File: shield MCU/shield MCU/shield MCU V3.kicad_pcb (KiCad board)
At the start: 2 copper layers, 56 x 75.2 mm, 17 parts, among them J1 IR_sensor, J2 IR_sensor, J3 IR_sensor, J4 IR_sensor, J5 IR_sensor, J6 BATT, SW1 Pwr_Sw, U1 pwr_mgr_1, U3 gy50, U4 NUCLEO144-F429ZI

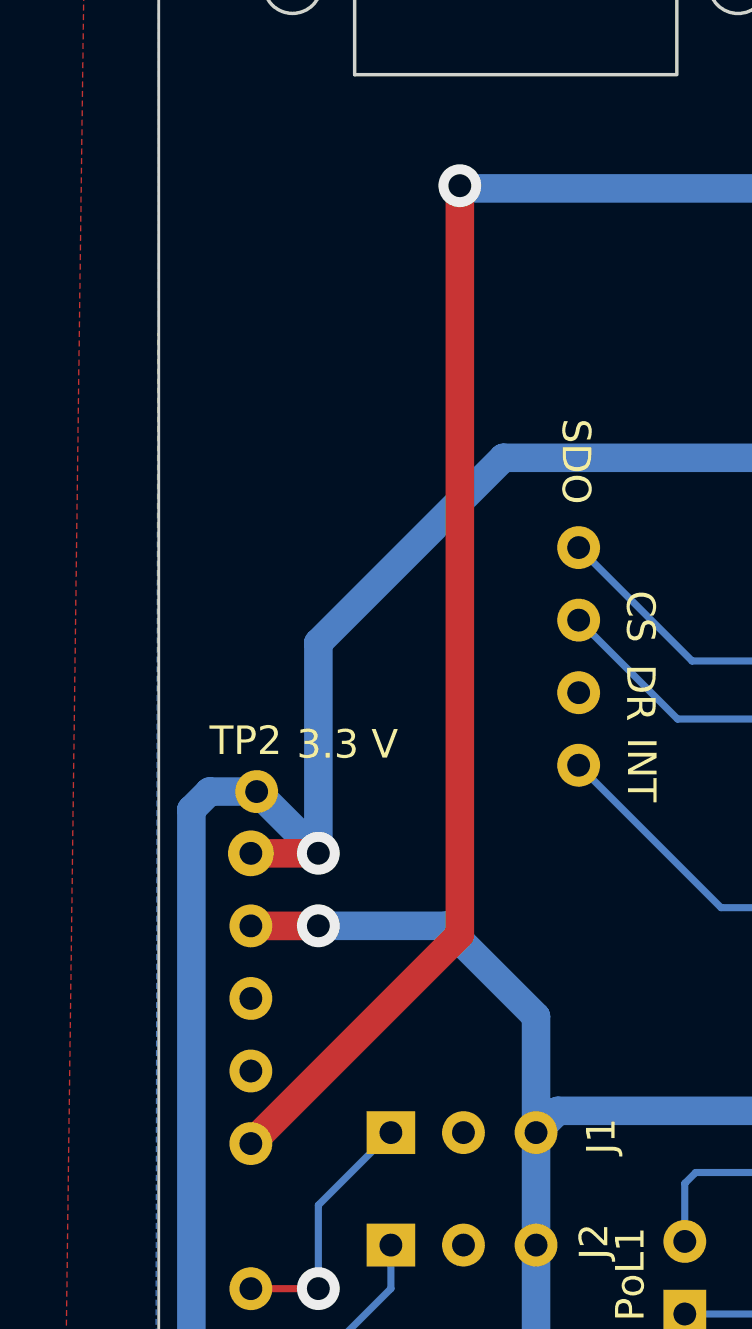
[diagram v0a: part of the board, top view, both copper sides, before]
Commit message: pcb V3 korjattu
ground korjattu
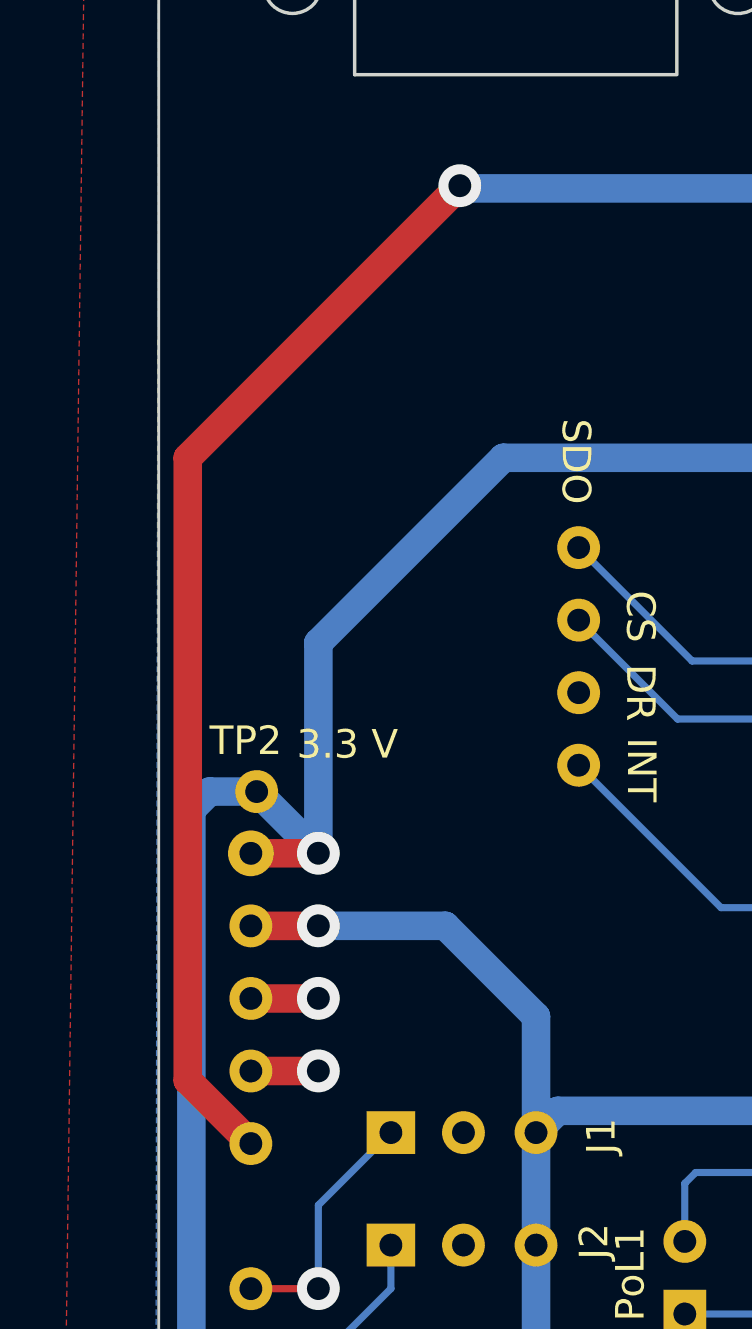
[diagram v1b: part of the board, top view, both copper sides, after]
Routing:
- net GND: track 0.00 -> 4.73 mm, vias 0 -> 2
- net /Vin: track 59.7 -> 61.6 mm
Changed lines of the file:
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@@
     (effects (font (size 1 1) (thickness 0.15)))
   )
+  (segment (start 108.582 110.366) (end 108.585 110.363) (width 1) (layer "F.Cu") (net 1))
+  (segment (start 106.2228 110.366) (end 108.582 110.366) (width 1) (layer "F.Cu") (net 1))
+  (segment (start 106.2228 107.826) (end 108.582 107.826) (width 1) (layer "F.Cu") (net 1))
+  (segment (start 108.582 107.826) (end 108.585 107.823) (width 1) (layer "F.Cu") (net 1))
+  (via (at 108.585 107.823) (size 1.5) (drill 0.8) (layers "F.Cu" "B.Cu") (free) (net 1))
+  (via (at 108.585 110.363) (size 1.5) (drill 0.8) (layers "F.Cu" "B.Cu") (free) (net 1))
   (segment (start 145.923 119.761) (end 146.431 119.253) (width 0.25) (layer "B.Cu") (net 2))
   (segment (start 141.097 119.761) (end 145.923 119.761) (width 0.25) (layer "B.Cu") (net 2))
@@
   (segment (start 132.207 115.1382) (end 132.207 113.157) (width 1) (layer "B.Cu") (net 13))
   (segment (start 132.207 113.157) (end 130.81 111.76) (width 1) (layer "B.Cu") (net 13))
-  (segment (start 113.538 105.5908) (end 106.2228 112.906) (width 1) (layer "F.Cu") (net 18))
-  (segment (start 113.538 79.375) (end 113.538 105.5908) (width 1) (layer "F.Cu") (net 18))
+  (segment (start 104.013 88.9) (end 113.538 79.375) (width 1) (layer "F.Cu") (net 18))
+  (segment (start 106.2228 112.906) (end 104.013 110.6962) (width 1) (layer "F.Cu") (net 18))
+  (segment (start 104.013 110.6962) (end 104.013 88.9) (width 1) (layer "F.Cu") (net 18))
   (via (at 113.538 79.375) (size 1.5) (drill 0.8) (layers "F.Cu" "B.Cu") (free) (net 18))
   (segment (start 113.633 79.47) (end 113.538 79.375) (width 1) (layer "B.Cu") (net 18))

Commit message: pcb pieni päivitys
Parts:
- moved TP2 0.36 mm to (106.2, 100.3)
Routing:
- net /3.3V: track 98.3 -> 97.2 mm
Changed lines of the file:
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@@
     (pad "4" thru_hole circle (at 15.367 -2.667 270) (size 1.5 1.5) (drill 0.8) (layers *.Cu *.Mask)
       (net 9 "Net-(U3-Pad4)") (pinfunction "INT") (pintype "output"))
-    (pad "5" thru_hole circle (at 7.747 -20.447 270) (size 1.5 1.5) (drill 0.8) (layers *.Cu *.Mask)
+    (pad "5" thru_hole roundrect (at 7.747 -20.447 270) (size 1.5 1.5) (drill 0.8) (layers *.Cu *.Mask) (roundrect_rratio 0.25)
       (net 4 "/3.3V") (pinfunction "VCC") (pintype "input"))
     (pad "6" thru_hole circle (at 10.287 -20.447 270) (size 1.5 1.5) (drill 0.8) (layers *.Cu *.Mask)
@@
   )
   (footprint "Connector_Pin:Pin_D0.7mm_L6.5mm_W1.8mm_FlatFork" (layer "F.Cu")
-    (at 106.426 100.584)
+    (at 106.172 100.33)
     (descr "solder Pin_ with flat fork, hole diameter 0.7mm, length 6.5mm, width 1.8mm")
     (tags "solder Pin_ with flat fork")
@@
   (segment (start 106.2228 102.746) (end 108.582 102.746) (width 1) (layer "F.Cu") (net 4))
   (via (at 108.585 102.743) (size 1.5) (drill 0.8) (layers "F.Cu" "B.Cu") (free) (net 4))
-  (segment (start 104.14 101.219) (end 104.14 132.334) (width 1) (layer "B.Cu") (net 4))
   (segment (start 132.334 88.9) (end 135.477 92.043) (width 1) (layer "B.Cu") (net 4))
-  (segment (start 106.426 100.584) (end 104.775 100.584) (width 1) (layer "B.Cu") (net 4))
+  (segment (start 104.14 102.87) (end 104.14 132.334) (width 1) (layer "B.Cu") (net 4))
   (segment (start 115.062 88.9) (end 132.334 88.9) (width 1) (layer "B.Cu") (net 4))
   (segment (start 108.585 95.377) (end 115.062 88.9) (width 1) (layer "B.Cu") (net 4))
   (segment (start 109.728 137.922) (end 122.809 137.922) (width 1) (layer "B.Cu") (net 4))
-  (segment (start 104.775 100.584) (end 104.14 101.219) (width 1) (layer "B.Cu") (net 4))
-  (segment (start 108.585 102.743) (end 106.426 100.584) (width 1) (layer "B.Cu") (net 4))
   (segment (start 104.14 132.334) (end 109.728 137.922) (width 1) (layer "B.Cu") (net 4))
-  (segment (start 108.585 102.743) (end 108.585 95.377) (width 1) (layer "B.Cu") (net 4))
+  (segment (start 108.585 102.743) (end 108.585 101.219) (width 1) (layer "B.Cu") (net 4))
+  (segment (start 107.696 100.33) (end 108.585 101.219) (width 1) (layer "B.Cu") (net 4))
+  (segment (start 104.14 102.362) (end 104.14 102.87) (width 1) (layer "B.Cu") (net 4))
+  (segment (start 108.585 101.219) (end 108.585 95.377) (width 1) (layer "B.Cu") (net 4))
+  (segment (start 106.172 100.33) (end 107.696 100.33) (width 1) (layer "B.Cu") (net 4))
+  (segment (start 106.172 100.33) (end 104.14 102.362) (width 1) (layer "B.Cu") (net 4))
   (segment (start 121.412 114.3) (end 121.793 113.919) (width 0.25) (layer "B.Cu") (net 5))
   (segment (start 121.793 113.919) (end 125.9078 113.919) (width 0.25) (layer "B.Cu") (net 5))
